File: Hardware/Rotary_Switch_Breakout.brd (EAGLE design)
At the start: 30.5 x 30.5 mm, 7 parts, among them SW1 1x10

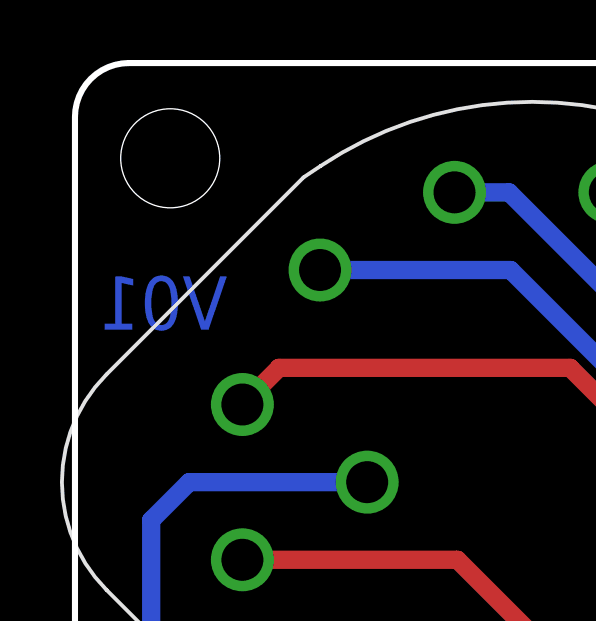
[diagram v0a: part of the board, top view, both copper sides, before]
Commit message: Ready to review for reds
Added dimensions, rolled revision # to V10
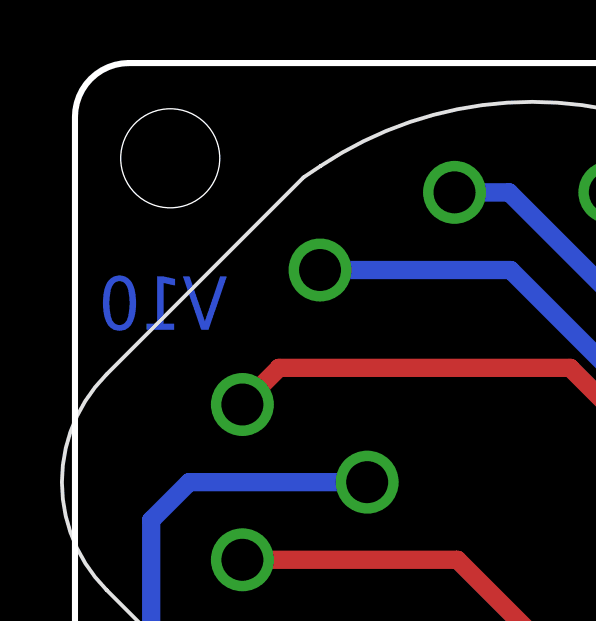
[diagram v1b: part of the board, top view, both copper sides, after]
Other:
- board text added: "V10"
- board text removed: "V01"
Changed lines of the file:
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@@
 <setting verticaltext="up"/>
 </settings>
-<grid distance="0.05" unitdist="inch" unit="inch" style="lines" multiple="1" display="yes" altdistance="0.005" altunitdist="inch" altunit="inch"/>
+<grid distance="0.05" unitdist="inch" unit="inch" style="lines" multiple="1" display="yes" altdistance="0.001" altunitdist="inch" altunit="inch"/>
 <layers>
 <layer number="1" name="Top" color="4" fill="1" visible="yes" active="yes"/>
@@
 <layer number="42" name="bRestrict" color="1" fill="10" visible="no" active="yes"/>
 <layer number="43" name="vRestrict" color="2" fill="10" visible="no" active="yes"/>
-<layer number="44" name="Drills" color="7" fill="1" visible="no" active="yes"/>
+<layer number="44" name="Drills" color="7" fill="1" visible="yes" active="yes"/>
 <layer number="45" name="Holes" color="7" fill="1" visible="yes" active="yes"/>
 <layer number="46" name="Milling" color="3" fill="1" visible="no" active="yes"/>
@@
 <text x="25.4" y="2.54" size="1.778" layer="22" font="vector" ratio="15" rot="MR90" align="center-left">9</text>
 <text x="27.94" y="2.54" size="1.778" layer="22" font="vector" ratio="15" rot="MR90" align="center-left">10</text>
-<text x="5.08" y="21.59" size="1.778" layer="16" font="vector" ratio="15" rot="MR0">V01</text>
+<text x="5.08" y="21.59" size="1.778" layer="16" font="vector" ratio="15" rot="MR0">V10</text>
+<wire x1="0" y1="30.48" x2="30.48" y2="30.48" width="0.2032" layer="51"/>
+<wire x1="30.48" y1="30.48" x2="30.48" y2="0" width="0.2032" layer="51"/>
+<wire x1="30.48" y1="0" x2="0" y2="0" width="0.2032" layer="51"/>
+<wire x1="0" y1="0" x2="0" y2="30.48" width="0.2032" layer="51"/>
+<dimension x1="0" y1="0" x2="0" y2="30.48" x3="-17.78" y3="15.24" textsize="1.778" textratio="15" layer="51" unit="inch" precision="4"/>
+<dimension x1="0" y1="30.48" x2="30.48" y2="30.48" x3="15.24" y3="49.53" textsize="1.778" textratio="15" layer="51" unit="inch" precision="4"/>
+<dimension x1="3.175" y1="27.305" x2="3.175" y2="30.48" x3="-10.16" y3="28.8925" textsize="1.778" textratio="15" layer="51" dtype="vertical" unit="inch" precision="4"/>
+<dimension x1="3.175" y1="27.305" x2="0" y2="27.305" x3="1.5875" y3="34.29" textsize="1.778" textratio="15" layer="51" dtype="vertical" unit="inch" precision="4"/>
+<dimension x1="30.48" y1="30.48" x2="27.305" y2="27.305" x3="44.45" y3="28.8925" textsize="1.778" textratio="15" layer="51" dtype="vertical" unit="inch" precision="4"/>
+<dimension x1="27.305" y1="27.305" x2="30.48" y2="27.305" x3="28.8925" y3="34.417" textsize="1.778" textratio="15" layer="51" unit="inch" precision="4"/>
+<dimension x1="15.24" y1="16.51" x2="0" y2="16.51" x3="7.62" y3="44.45" textsize="1.778" textratio="15" layer="51" unit="inch" precision="4"/>
+<dimension x1="15.24" y1="16.51" x2="15.24" y2="0" x3="-6.35" y3="8.255" textsize="1.778" textratio="15" layer="51" unit="inch" precision="4"/>
+<dimension x1="28.4988" y1="28.448" x2="26.1366" y2="26.1112" x3="41.46330625" y3="12.9802375" textsize="1.778" textratio="15" layer="51" unit="inch" precision="4"/>
 </plain>
 <attributes>

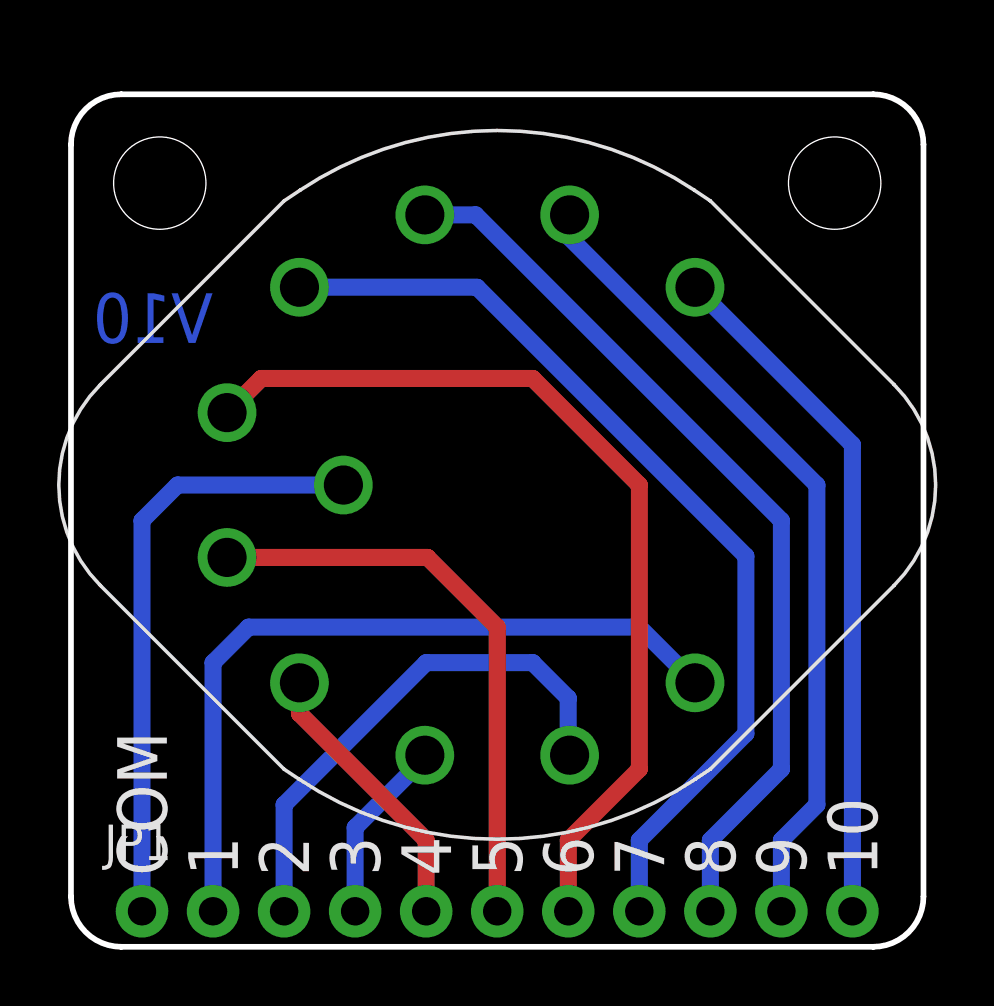
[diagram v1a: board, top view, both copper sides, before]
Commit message: Revising from review comments.
Now has 4 standoff holes.
Dimensioning is more legible.
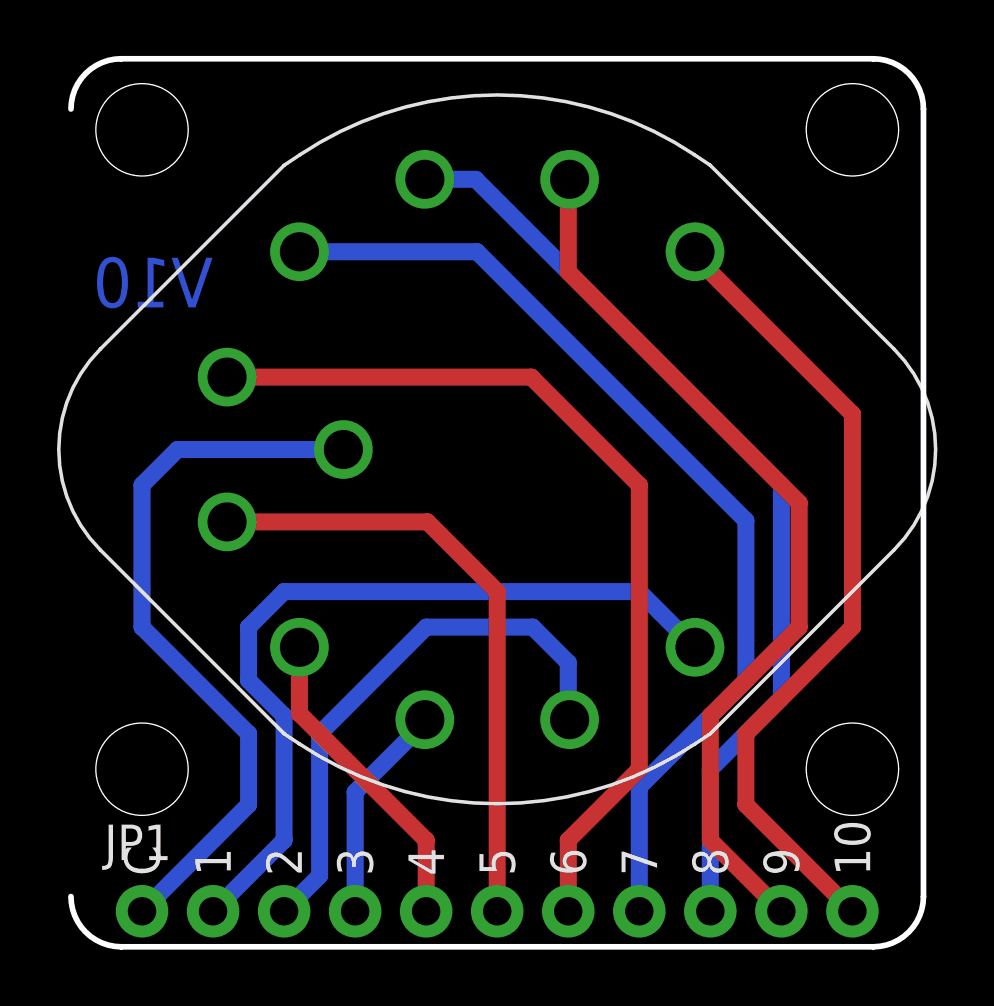
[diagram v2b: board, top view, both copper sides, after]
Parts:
- added STANDOFF3, STANDOFF4: STAND-OFF, SparkFun-Electromechanical:STAND-OFF
- moved STANDOFF2 2.01 mm to (27.9, 29.2)
- moved STANDOFF1 2.01 mm to (2.54, 29.2)
- moved LOGO3 1.27 mm to (21.3, 8.89)
- moved LOGO1 1.27 mm to (15.2, 15.2)
- moved SW1 1.27 mm to (15.2, 17.8)
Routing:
- net N$11: track 24.6 -> 29.1 mm
- net N$1: track 21.7 -> 26.1 mm
- net N$10: track 29.1 -> 32.0 mm
- net N$2: track 27.5 -> 29.1 mm
- net N$5: track 10.0 -> 11.3 mm
- net N$3: track 18.7 -> 19.9 mm
- net N$4: track 6.68 -> 7.95 mm
- net N$9: track 32.3 -> 33.6 mm
- net N$8: track 34.2 -> 35.5 mm
- net N$6: track 20.9 -> 22.1 mm
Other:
- board size 30.5 x 30.5 mm -> 30.5 x 31.8 mm
- board text added: "0.125(4-40)"
- board text added: "C"
- board text removed: "COM"

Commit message: Updated from QC checklist review.
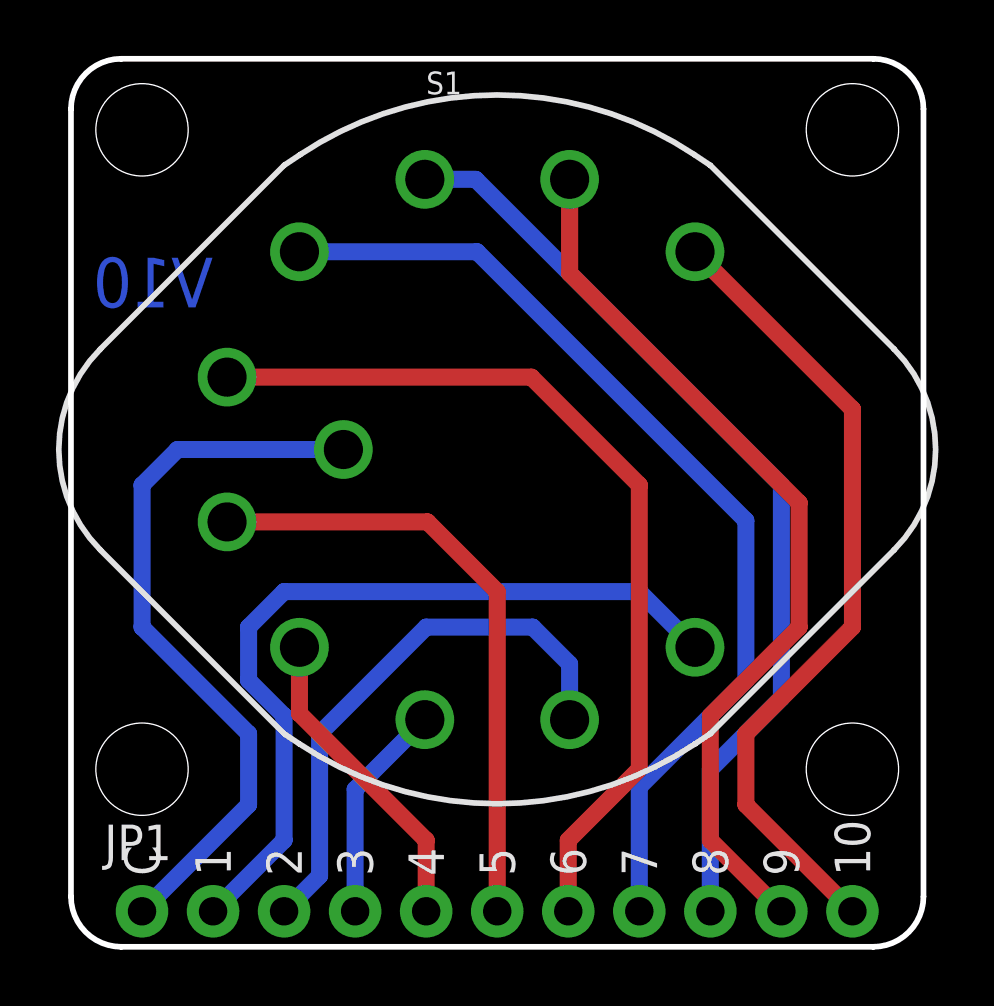
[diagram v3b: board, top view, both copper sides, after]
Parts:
- renumbered SW1 to S1
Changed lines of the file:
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@@
 <setting verticaltext="up"/>
 </settings>
-<grid distance="0.05" unitdist="inch" unit="inch" style="lines" multiple="1" display="yes" altdistance="0.025" altunitdist="inch" altunit="inch"/>
+<grid distance="0.05" unitdist="inch" unit="inch" style="lines" multiple="1" display="yes" altdistance="0.005" altunitdist="inch" altunit="inch"/>
 <layers>
 <layer number="1" name="Top" color="4" fill="1" visible="yes" active="yes"/>
@@
 <layer number="23" name="tOrigins" color="15" fill="1" visible="yes" active="yes"/>
 <layer number="24" name="bOrigins" color="15" fill="1" visible="yes" active="yes"/>
-<layer number="25" name="tNames" color="7" fill="1" visible="no" active="yes"/>
-<layer number="26" name="bNames" color="7" fill="1" visible="no" active="yes"/>
+<layer number="25" name="tNames" color="7" fill="1" visible="yes" active="yes"/>
+<layer number="26" name="bNames" color="7" fill="1" visible="yes" active="yes"/>
 <layer number="27" name="tValues" color="7" fill="1" visible="no" active="yes"/>
 <layer number="28" name="bValues" color="7" fill="1" visible="no" active="yes"/>
@@
 <layer number="37" name="tTest" color="7" fill="1" visible="no" active="yes"/>
 <layer number="38" name="bTest" color="7" fill="1" visible="no" active="yes"/>
-<layer number="39" name="tKeepout" color="4" fill="11" visible="yes" active="yes"/>
+<layer number="39" name="tKeepout" color="4" fill="11" visible="no" active="yes"/>
 <layer number="40" name="bKeepout" color="1" fill="11" visible="no" active="yes"/>
 <layer number="41" name="tRestrict" color="4" fill="10" visible="no" active="yes"/>
@@
 <layer number="43" name="vRestrict" color="2" fill="10" visible="no" active="yes"/>
 <layer number="44" name="Drills" color="7" fill="1" visible="no" active="yes"/>
-<layer number="45" name="Holes" color="7" fill="1" visible="yes" active="yes"/>
+<layer number="45" name="Holes" color="7" fill="1" visible="no" active="yes"/>
 <layer number="46" name="Milling" color="3" fill="1" visible="no" active="yes"/>
 <layer number="47" name="Measures" color="7" fill="1" visible="no" active="yes"/>
@@
 <layer number="49" name="Reference" color="7" fill="1" visible="no" active="yes"/>
 <layer number="50" name="dxf" color="7" fill="1" visible="no" active="no"/>
-<layer number="51" name="tDocu" color="6" fill="1" visible="yes" active="yes"/>
+<layer number="51" name="tDocu" color="6" fill="1" visible="no" active="yes"/>
 <layer number="52" name="bDocu" color="7" fill="1" visible="no" active="yes"/>
 <layer number="53" name="tGND_GNDA" color="7" fill="9" visible="no" active="no"/>
@@
 <text x="25.4" y="2.54" size="1.27" layer="21" font="vector" ratio="15" rot="R90" align="center-left">9</text>
 <text x="27.94" y="2.54" size="1.27" layer="21" font="vector" ratio="15" rot="R90" align="center-left">10</text>
-<text x="15.24" y="24.892" size="1.778" layer="22" font="vector" ratio="15" rot="MR0" align="top-center">1x10
+<text x="15.24" y="26.162" size="1.778" layer="22" font="vector" ratio="15" rot="MR0" align="top-center">1x10
 Rotary Switch
 Breakout</text>
@@
 <dimension x1="27.94" y1="29.21" x2="34.29" y2="34.29" x3="39.37" y3="34.29" textsize="1.778" textratio="15" layer="51" dtype="leader" unit="inch"/>
 <text x="39.37" y="34.29" size="1.778" layer="51" ratio="15">0.125(4-40)</text>
+<wire x1="0" y1="1.79605" x2="0" y2="29.95395" width="0.2032" layer="20"/>
 </plain>
 <attributes>
@@
 <elements>
 <element name="FRAME1" library="SparkFun-Aesthetics" package="CREATIVE_COMMONS" value="FRAME-LETTER" x="0" y="-7.62"/>
-<element name="SW1" library="SparkFun-Electromechanical" package="ROTARY_SWITCH_1X10_KIT" value="1x10" x="15.24" y="17.78" rot="R270">
+<element name="S1" library="SparkFun-Electromechanical" package="ROTARY_SWITCH_1X10_KIT" value="1x10" x="15.24" y="17.78" rot="R270">
 <attribute name="PROD_ID" value="SWCH-12120" x="-1.27" y="-8.89" size="1.778" layer="27" rot="R270" display="off"/>
 </element>
@@
 <signal name="N$1">
 <contactref element="JP1" pad="1"/>
-<contactref element="SW1" pad="COMMON"/>
+<contactref element="S1" pad="COMMON"/>
 <wire x1="2.54" y1="1.27" x2="6.35" y2="5.08" width="0.6096" layer="16"/>
 <wire x1="6.35" y1="5.08" x2="6.35" y2="7.62" width="0.6096" layer="16"/>
@@
 <signal name="N$2">
 <contactref element="JP1" pad="2"/>
-<contactref element="SW1" pad="1"/>
+<contactref element="S1" pad="1"/>
 <wire x1="5.08" y1="1.27" x2="7.62" y2="3.81" width="0.6096" layer="16"/>
 <wire x1="7.62" y1="3.81" x2="7.62" y2="8.255" width="0.6096" layer="16"/>
@@
 </signal>
 <signal name="N$3">
-<contactref element="SW1" pad="2"/>
+<contactref element="S1" pad="2"/>
 <contactref element="JP1" pad="3"/>
 <wire x1="7.62" y1="1.27" x2="8.89" y2="2.54" width="0.6096" layer="16"/>
@@
 <wire x1="8.89" y1="7.62" x2="12.7" y2="11.43" width="0.6096" layer="16"/>
 <wire x1="12.7" y1="11.43" x2="16.51" y2="11.43" width="0.6096" layer="16"/>
-<wire x1="16.51" y1="11.43" x2="17.78" y2="10.16" width="0.6096" layer="16"/>
-<wire x1="17.78" y1="10.16" x2="17.78" y2="8.16893125" width="0.6096" layer="16"/>
-<wire x1="17.78" y1="8.16893125" x2="17.828190625" y2="8.120740625" width="0.6096" layer="16"/>
+<wire x1="17.828190625" y1="8.120740625" x2="17.828190625" y2="10.111809375" width="0.6096" layer="16"/>
+<wire x1="17.828190625" y1="10.111809375" x2="16.51" y2="11.43" width="0.6096" layer="16"/>
 </signal>
 <signal name="N$4">
 <contactref element="JP1" pad="4"/>
-<contactref element="SW1" pad="3"/>
-<wire x1="10.16" y1="1.27" x2="10.16" y2="5.53255" width="0.6096" layer="16"/>
-<wire x1="12.7" y1="8.07255" x2="12.651809375" y2="8.024359375" width="0.6096" layer="16"/>
-<wire x1="12.651809375" y1="8.024359375" x2="10.16" y2="5.53255" width="0.6096" layer="16"/>
-<wire x1="12.651809375" y1="8.120740625" x2="12.651809375" y2="8.024359375" width="0.6096" layer="16"/>
+<contactref element="S1" pad="3"/>
+<wire x1="10.16" y1="1.27" x2="10.16" y2="5.62893125" width="0.6096" layer="16"/>
+<wire x1="12.651809375" y1="8.120740625" x2="10.16" y2="5.62893125" width="0.6096" layer="16"/>
 </signal>
 <signal name="N$5">
 <contactref element="JP1" pad="5"/>
-<contactref element="SW1" pad="4"/>
+<contactref element="S1" pad="4"/>
 <wire x1="12.7" y1="1.27" x2="12.7" y2="3.81" width="0.6096" layer="1"/>
 <wire x1="12.7" y1="3.81" x2="8.16893125" y2="8.34106875" width="0.6096" layer="1"/>
@@
 <signal name="N$6">
 <contactref element="JP1" pad="6"/>
-<contactref element="SW1" pad="5"/>
+<contactref element="S1" pad="5"/>
 <wire x1="5.580740625" y1="15.191809375" x2="12.748190625" y2="15.191809375" width="0.6096" layer="1"/>
 <wire x1="12.748190625" y1="15.191809375" x2="15.24" y2="12.7" width="0.6096" layer="1"/>
@@
 <signal name="N$7">
 <contactref element="JP1" pad="7"/>
-<contactref element="SW1" pad="6"/>
+<contactref element="S1" pad="6"/>
 <wire x1="17.78" y1="1.27" x2="17.78" y2="3.81" width="0.6096" layer="1"/>
 <wire x1="17.78" y1="3.81" x2="20.32" y2="6.35" width="0.6096" layer="1"/>
@@
 <signal name="N$8">
 <contactref element="JP1" pad="8"/>
-<contactref element="SW1" pad="7"/>
+<contactref element="S1" pad="7"/>
 <wire x1="8.16893125" y1="24.85106875" x2="14.51893125" y2="24.85106875" width="0.6096" layer="16"/>
 <wire x1="14.51893125" y1="24.85106875" x2="24.13" y2="15.24" width="0.6096" layer="16"/>
@@
 <signal name="N$9">
 <contactref element="JP1" pad="9"/>
-<contactref element="SW1" pad="8"/>
+<contactref element="S1" pad="8"/>
 <wire x1="22.86" y1="1.27" x2="22.86" y2="6.35" width="0.6096" layer="16"/>
 <wire x1="22.86" y1="6.35" x2="25.4" y2="8.89" width="0.6096" layer="16"/>
@@
 </signal>
 <signal name="N$10">
-<contactref element="SW1" pad="9"/>
+<contactref element="S1" pad="9"/>
 <contactref element="JP1" pad="10"/>
 <wire x1="25.4" y1="1.27" x2="22.86" y2="3.81" width="0.6096" layer="1"/>
@@
 <wire x1="22.86" y1="8.255" x2="26.035" y2="11.43" width="0.6096" layer="1"/>
 <wire x1="26.035" y1="11.43" x2="26.035" y2="15.875" width="0.6096" layer="1"/>
-<wire x1="26.035" y1="15.875" x2="17.78" y2="24.13" width="0.6096" layer="1"/>
-<wire x1="17.78" y1="24.13" x2="17.78" y2="27.39106875" width="0.6096" layer="1"/>
-<wire x1="17.78" y1="27.39106875" x2="17.828190625" y2="27.439259375" width="0.6096" layer="1"/>
+<wire x1="17.828190625" y1="27.439259375" x2="17.828190625" y2="24.081809375" width="0.6096" layer="1"/>
+<wire x1="17.828190625" y1="24.081809375" x2="26.035" y2="15.875" width="0.6096" layer="1"/>
 </signal>
 <signal name="N$11">
 <contactref element="JP1" pad="11"/>
-<contactref element="SW1" pad="10"/>
+<contactref element="S1" pad="10"/>
 <wire x1="27.94" y1="1.27" x2="24.13" y2="5.08" width="0.6096" layer="1"/>
 <wire x1="24.13" y1="5.08" x2="24.13" y2="7.62" width="0.6096" layer="1"/>
 <wire x1="24.13" y1="7.62" x2="27.94" y2="11.43" width="0.6096" layer="1"/>
-<wire x1="27.94" y1="11.43" x2="27.94" y2="19.05" width="0.6096" layer="1"/>
-<wire x1="22.31106875" y1="24.85106875" x2="22.31106875" y2="24.67893125" width="0.6096" layer="1"/>
-<wire x1="22.31106875" y1="24.67893125" x2="27.94" y2="19.05" width="0.6096" layer="1"/>
+<wire x1="27.94" y1="11.43" x2="27.94" y2="19.2221375" width="0.6096" layer="1"/>
+<wire x1="22.31106875" y1="24.85106875" x2="27.94" y2="19.2221375" width="0.6096" layer="1"/>
 </signal>
 </signals>
